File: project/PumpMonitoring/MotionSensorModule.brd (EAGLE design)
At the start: 46 x 22 mm, 11 parts, among them CN1 JST-PH-K*, IC1 LSM9DS1

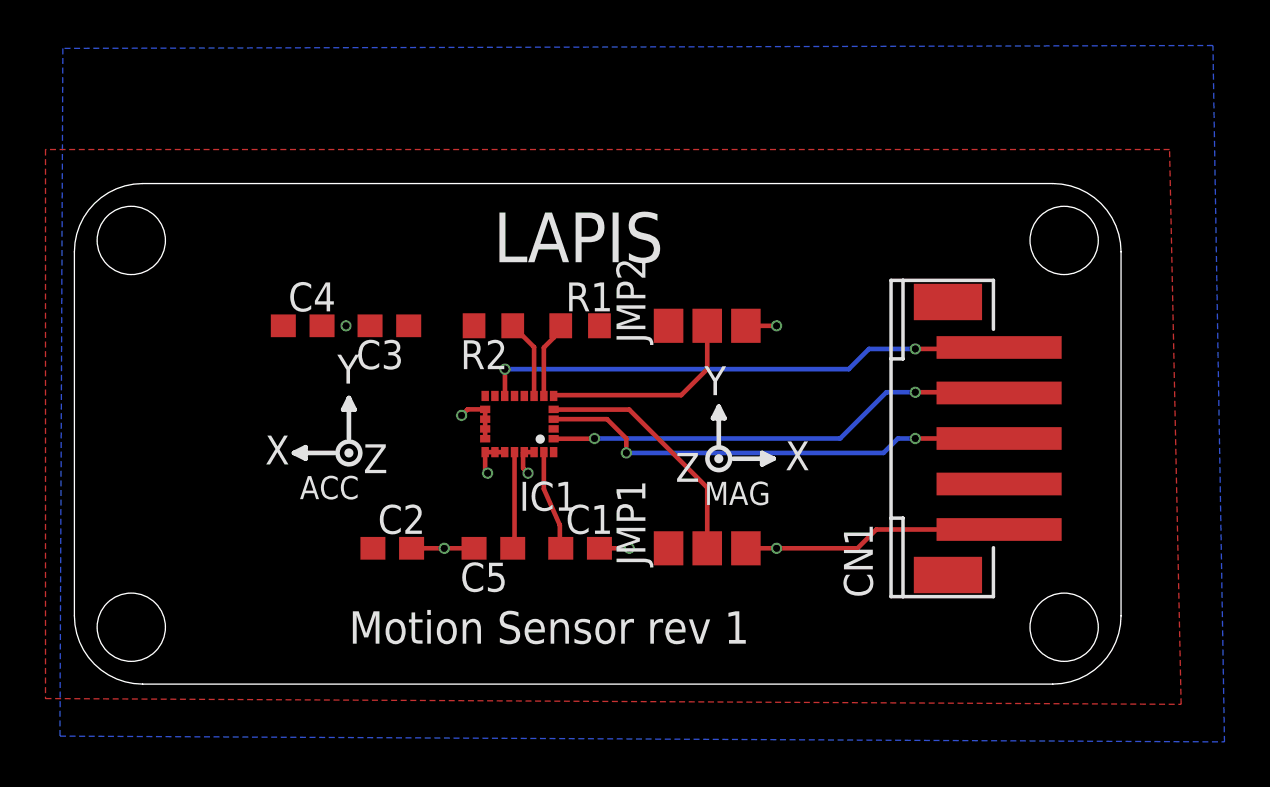
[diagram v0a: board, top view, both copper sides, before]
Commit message: add ti.lbr and update motion/sound module
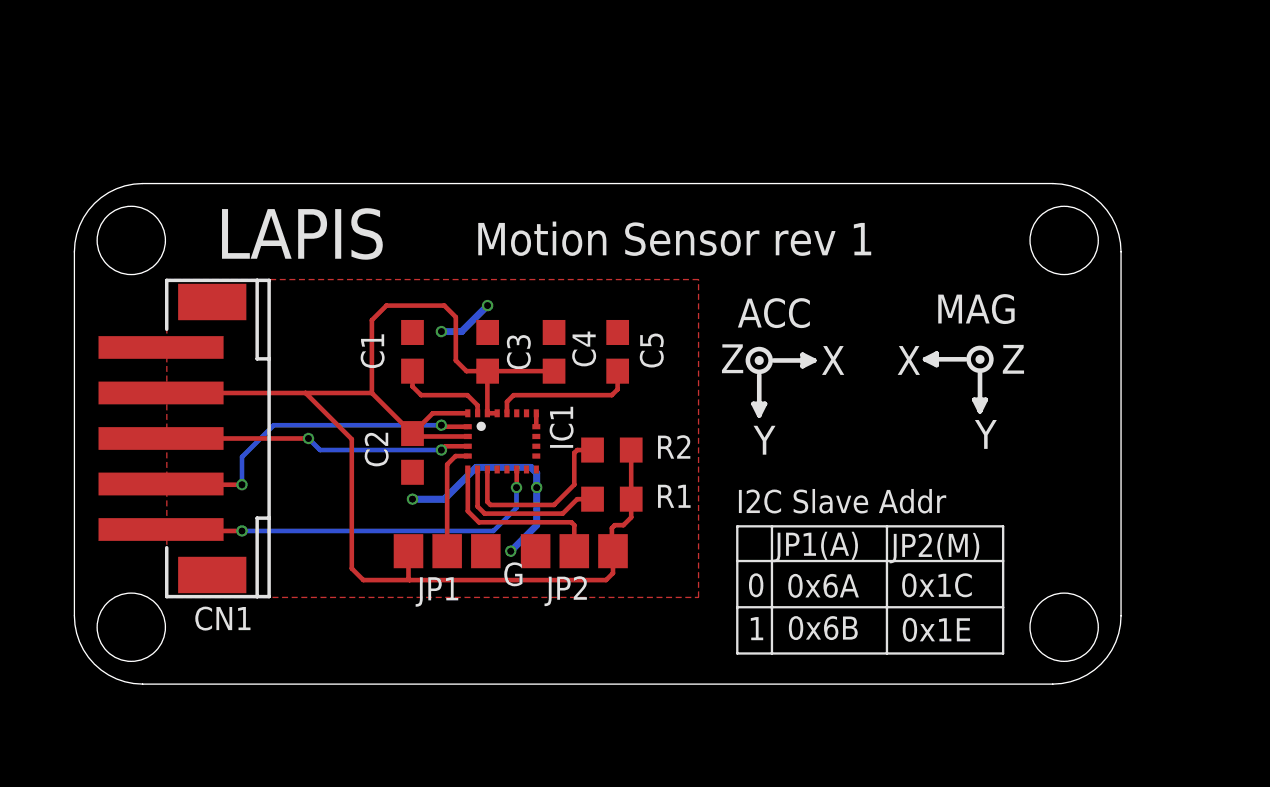
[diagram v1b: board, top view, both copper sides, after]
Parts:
- removed JMP1, JMP2: 0R-JUMPB, jump-0r-smd:B0R-JMP
- added JP1, JP2: 0R-JUMPB, jump-0r-smd:B0R-JMP
- moved CN1 30.7 mm to (6.86, 10.8), turned to 270 degrees
- moved C1 11.4 mm to (14.9, 14.6), turned to 90 degrees
- moved C4 11.1 mm to (21.1, 14.6), turned to 90 degrees
- moved C5 10.2 mm to (23.9, 14.6), turned to 90 degrees
- moved R1 7.75 mm to (23.6, 8.13)
- moved R2 7.55 mm to (23.6, 10.3), turned to 0 degrees
- moved C3 4.47 mm to (18.2, 14.6), turned to 90 degrees
- moved C2 4.28 mm to (14.9, 10.2), turned to 270 degrees
- moved IC1 1.08 mm to (18.8, 10.7), turned to 0 degrees
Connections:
- net GND: now also JP1.3, JP2.3; no longer JMP1.3, JMP2.3
- net N$4: now also JP1.2; no longer JMP1.2
- net N$6: now also JP2.2; no longer JMP2.2
- net VDD: now also JP1.1, JP2.1; no longer JMP1.1, JMP2.1
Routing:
- net VDD: track 1.50 -> 60.8 mm, vias 1 -> 0
- net GND: track 21.1 -> 13.1 mm, vias 7 -> 5
- net SDA: track 20.8 -> 13.8 mm
- net N$4: track 10.8 -> 4.87 mm
- net INT_G: track 23.3 -> 17.8 mm
- net SCL: track 20.4 -> 15.3 mm
- net N$2: track 3.47 -> 7.92 mm
- net N$3: track 3.39 -> 7.07 mm
- net N$7: track 4.30 -> 6.40 mm
- net N$6: track 9.14 -> 7.91 mm
- added copper zone on layer 1, net GND
- removed copper zone on layer 16, net GND
- removed copper zone on layer 1, net VDD
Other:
- board text added: "0"
- board text added: "0x1C"
- board text added: "0x1E"
- board text added: "0x6A"
- board text added: "0x6B"
- board text added: "1"
- board text added: "G"
- board text added: "I2C Slave Addr"
- board text added: "JP1(A)"
- board text added: "JP2(M)"

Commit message: update project of pump monitoring incl. sound and motion.
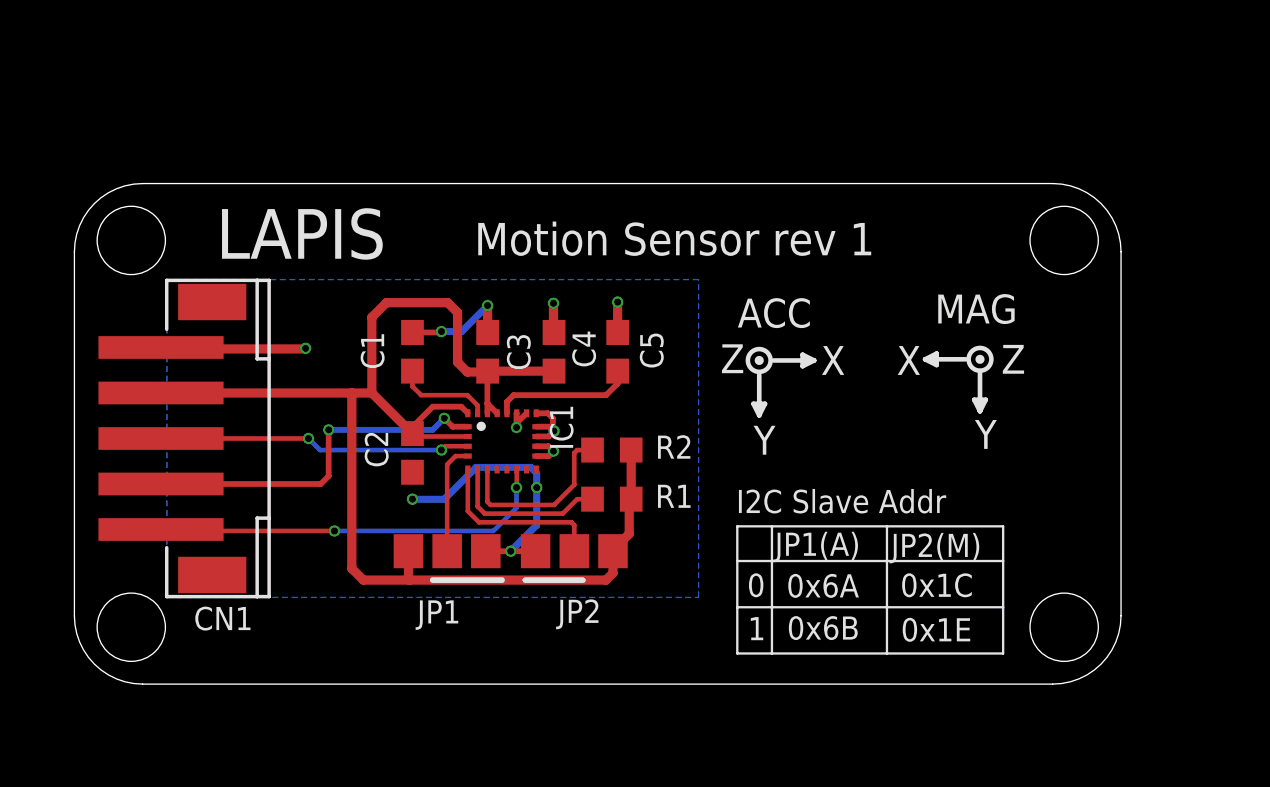
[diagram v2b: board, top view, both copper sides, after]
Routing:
- net GND: track 13.1 -> 32.5 mm, vias 5 -> 11
- net SCL: track 15.3 -> 16.0 mm
- added copper zone on layer 16, net GND
- removed copper zone on layer 1, net GND
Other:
- board text removed: "G"
